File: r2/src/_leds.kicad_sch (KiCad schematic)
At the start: 20 parts

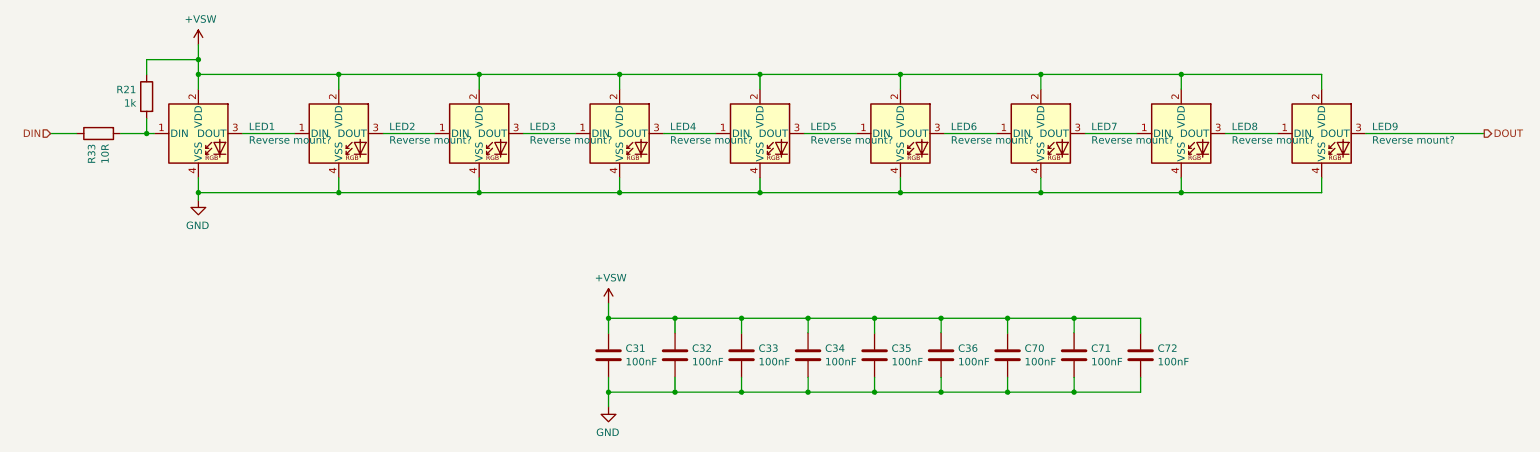
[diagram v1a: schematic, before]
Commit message: Fix off-grid ERC errors so whole schematic is on 1.27mm grid
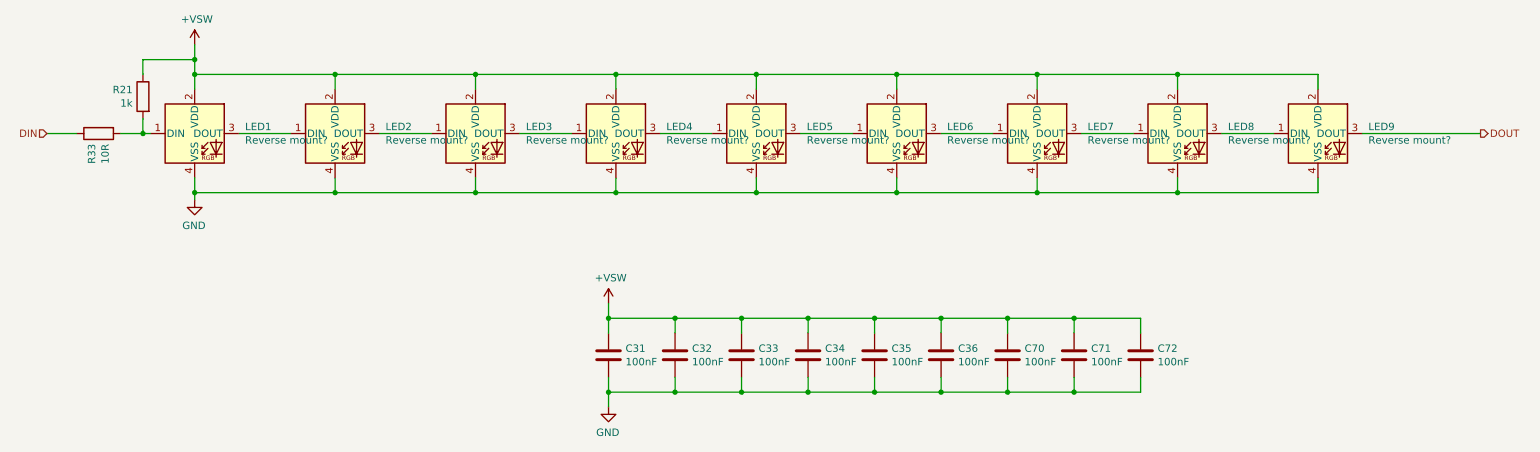
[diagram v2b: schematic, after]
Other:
- moved on the sheet: LED1, LED2, LED3, LED4, LED5, LED6, LED7, LED8, LED9, R21

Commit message: Add BOM info for side-firing SK LED's
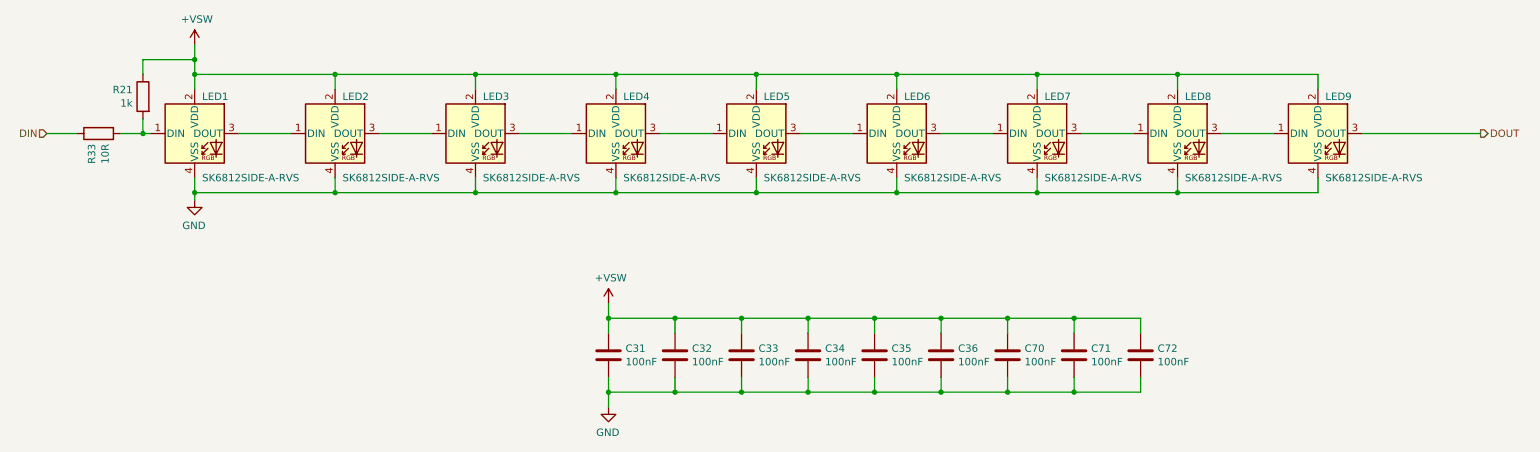
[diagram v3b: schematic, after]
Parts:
- LED1, LED2, LED3, LED4, LED5, LED6, LED7, LED8, LED9: value Reverse mount? -> SK6812SIDE-A-RVS; LCSC (none) -> C2890037; MPN (none) -> SK6812SIDE-A-RVS; Manufacturer (none) -> OPSCO Optoelectronics

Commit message: Set title block contents
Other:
- company: (none) -> Monad Gottfried Ltd. 2023
- title: (none) -> Troopers 23 Badge
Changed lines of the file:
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@@
 (kicad_sch (version 20230409) (generator eeschema)
   (paper "A4")
+  (title_block
+    (title "Troopers 23 Badge")
+    (rev "r2")
+    (company "Monad Gottfried Ltd. 2023")
+    (comment 1 "for ERNW Enno Rey Netzwerke GmbH")
+  )
   (junction (at 99.06 72.39) (diameter 0) (color 0 0 0 0)
   )
